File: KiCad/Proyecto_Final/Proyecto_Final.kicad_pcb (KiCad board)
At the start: 4 copper layers, 102 x 102 mm, 235 parts, among them J1 RF_IN, J10 PF, J11 PB, J12 PE, J13 PA, J14 PD, J15 SPI4, J16 OutEn, J17 CFG_SEL, J18 CTRL_MODE, J2 ADC_CLK_SEL, J3 5v, J4 I2C1, J5 ARM SWD, J6 USB_B_Micro, J7 Boot_Select, J8 PG, J9 PC, Q1 BSS315P, SW1 Reset, T1 B0310J50100AHF, T2 B0310J50100AHF, T3 2450BL05A0100, U1 SKY13351, U10 MAX2837, U11 TLV1117-33, U12 TPD4S012DRYR, U13 STM32F723ZCTx, U14 5P49V5929, U2 RFFC5072, U3 SKY13351, U4 SKY13351, U5 SKY13351, U6 SKY13351, U7 SKY13351, U8 MAAL-010200, U9 MAX1193ETI+, Y1 25MHz

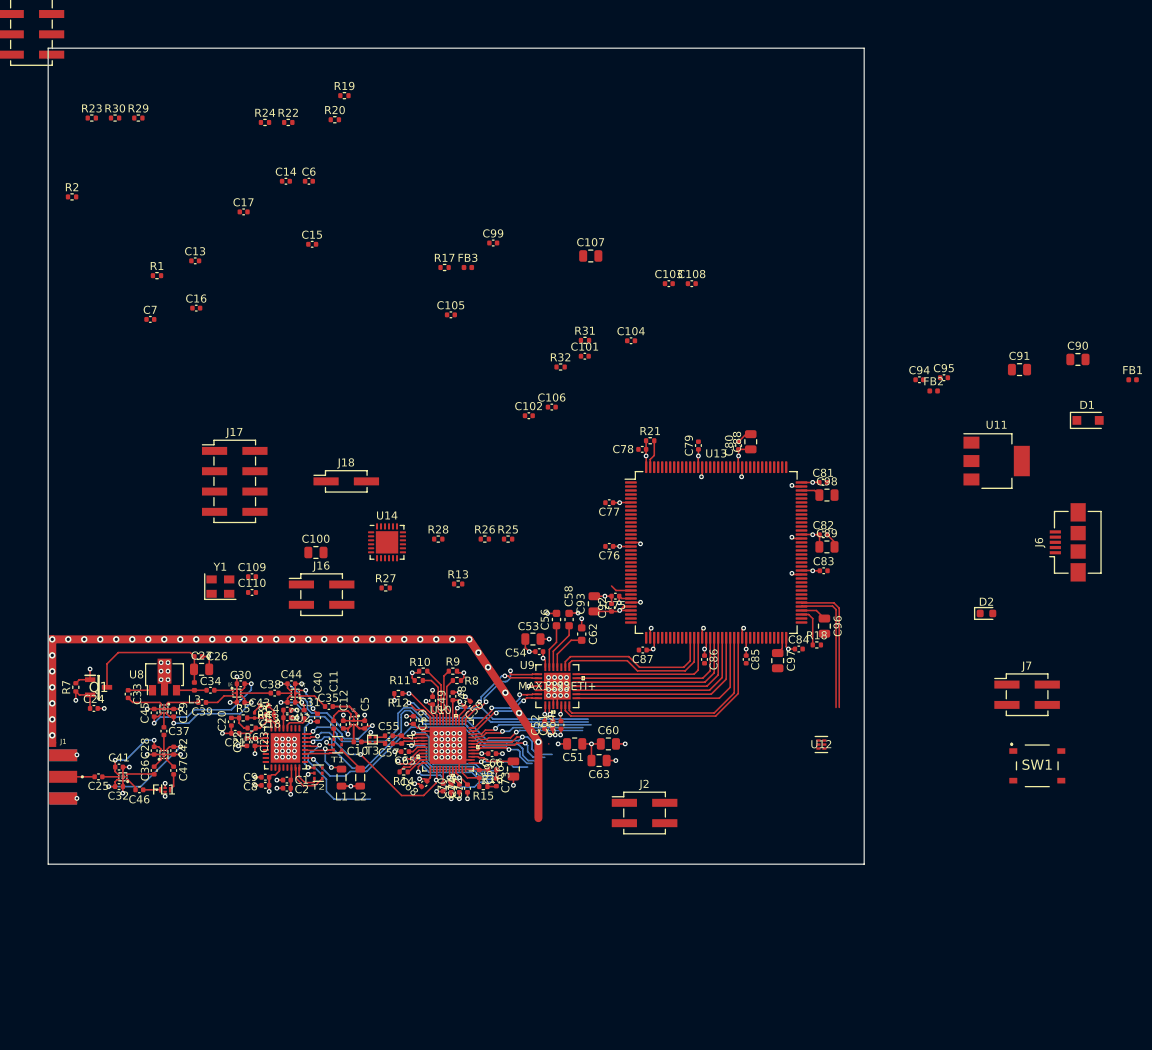
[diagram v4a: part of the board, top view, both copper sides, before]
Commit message: Reasignación de footprints por cambio de proveedor de componentes (JLCPCB SMT Assembly).
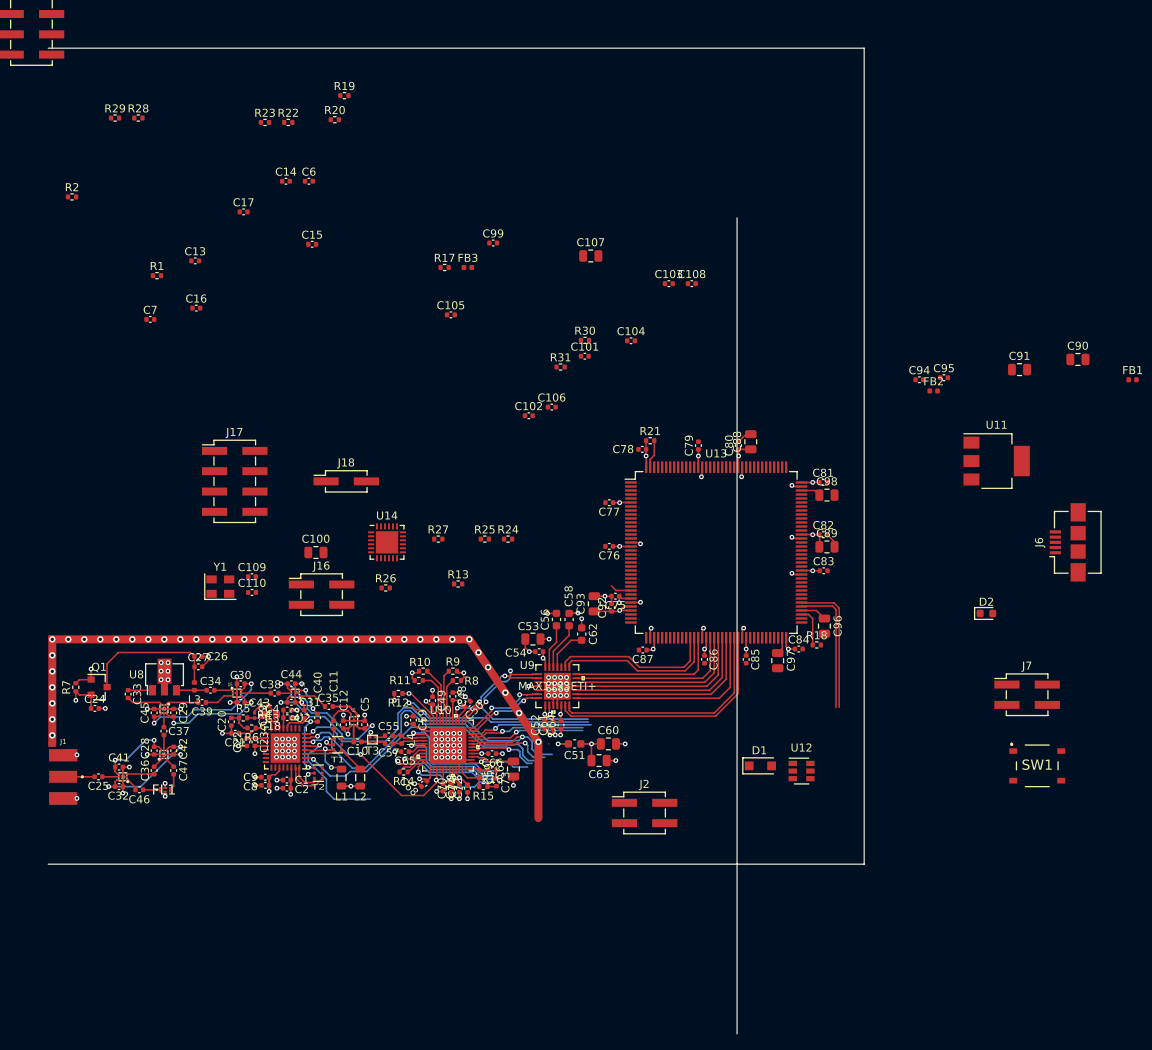
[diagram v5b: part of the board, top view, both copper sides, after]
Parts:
- removed the R23 at (81.2, 53.6)
- C18: footprint Capacitor_SMD:C_0402_1005Metric -> Capacitor_SMD:C_0603_1608Metric
- C27: footprint Capacitor_SMD:C_0805_2012Metric -> Capacitor_SMD:C_0402_1005Metric
- C51: footprint Capacitor_SMD:C_0805_2012Metric -> Capacitor_SMD:C_0603_1608Metric
- C52, C54, C61, C64: value 0.1uF -> 100nF
- D1: value PMEG2010EH -> SM4007
- FB1: value 120 @ 100MHz -> 600 @ 100MHz
- FB2, FB3: value 220 @ 100MHz -> 600 @ 100MHz
- Q1: value BSS315P -> Si2301CDS; footprint SamacSys_Parts:SOT95P237X112-3N -> Package_TO_SOT_SMD:SOT-23
- U12: value TPD4S012DRYR -> USBLC6-2SC6; footprint Tesis2020-21:TPD4S012DRYR -> Package_TO_SOT_SMD:SOT-23-6
- moved D1 59.5 mm to (164.8, 134.6)
- moved U12 4.14 mm to (169.9, 135.3)
- moved C27 0.52 mm to (94.5, 122.2)
- moved C24 0.13 mm to (81.6, 127.4)
- moved Q1 0.07 mm to (82.1, 124.8)
- renumbered R24 to R23, R25 to R24, R26 to R25, R27 to R26, R28 to R27, R29 to R28, R30 to R29, R31 to R30, R32 to R31
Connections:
- C100 pad 1: VDD_CLK -> VDDA_CLK
- C101 pad 1: VDD_CLK -> VDDA_CLK
- C102 pad 1: VDD_CLK -> VDDA_CLK
- C103 pad 1: VDD_CLK -> VDDA_CLK
- C104 pad 1: VDD_CLK -> VDDA_CLK
- C105 pad 1: VDD_CLK -> VDDA_CLK
- C106 pad 1: VDD_CLK -> VDDA_CLK
- FB1 pad 2: VBUS -> +5V
- FB3 pad 1: VDD_CLK -> VDDA_CLK
- J3 pad 1: VBUS -> +5V
- J6 pad 1: VBUS -> +5V
- J6 pad 2: USB_OTG_HS_D- -> USB_CONN_D-
- J6 pad 3: USB_OTG_HS_D+ -> USB_CONN_D+
- TP18 pad 1: VBUS -> +5V
- U12 pad 1: USB_OTG_HS_D+ -> USB_CONN_D+
- U12 pad 2: USB_OTG_HS_D- -> GND
- U12 pad 3: Net-(J6-Pad4) -> USB_CONN_D-
- U12 pad 4: GND -> USB_D-
- U12 pad 5: Net-(U12-Pad5) -> +5V
- U12 pad 6: VBUS -> USB_D+
- U13 pad 77: USB_OTG_HS_D- -> USB_D-
- U13 pad 78: USB_OTG_HS_D+ -> USB_D+
- U14 pad 10: VDD_CLK -> VDDA_CLK
- U14 pad 15: VDD_CLK -> VDDA_CLK
- U14 pad 18: VDD_CLK -> VDDA_CLK
- U14 pad 21: VDD_CLK -> VDDA_CLK
- U14 pad 22: VDD_CLK -> VDDA_CLK
- U14 pad 23: VDD_CLK -> VDDA_CLK
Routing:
- net USB_OTG_HS_D+: track 17.4 -> 0.00 mm
- net USB_D+: track 0.00 -> 17.4 mm
- net USB_OTG_HS_D-: track 16.7 -> 0.00 mm
- net USB_D-: track 0.00 -> 16.7 mm
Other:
- board size 102 x 102 mm -> 102 x 123.2 mm

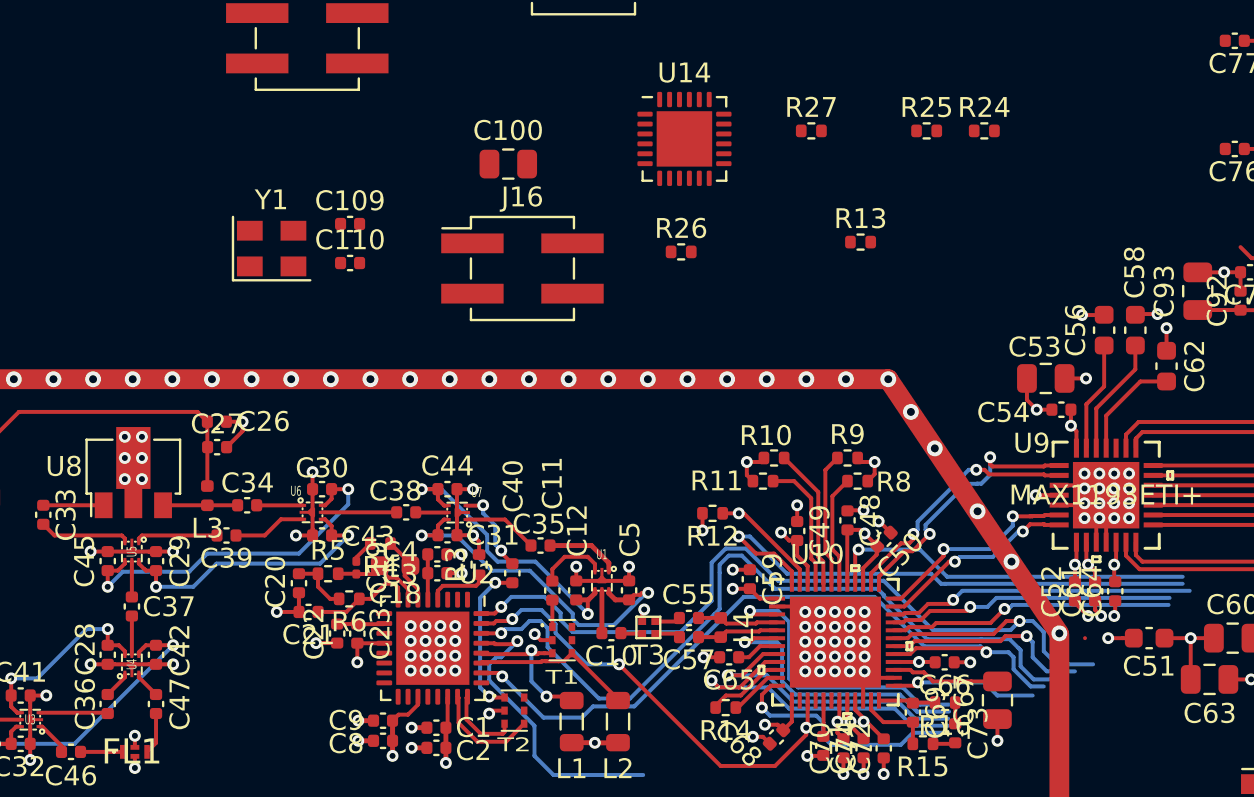
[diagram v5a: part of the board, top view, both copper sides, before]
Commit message: Agregada seccion de thermal vias.
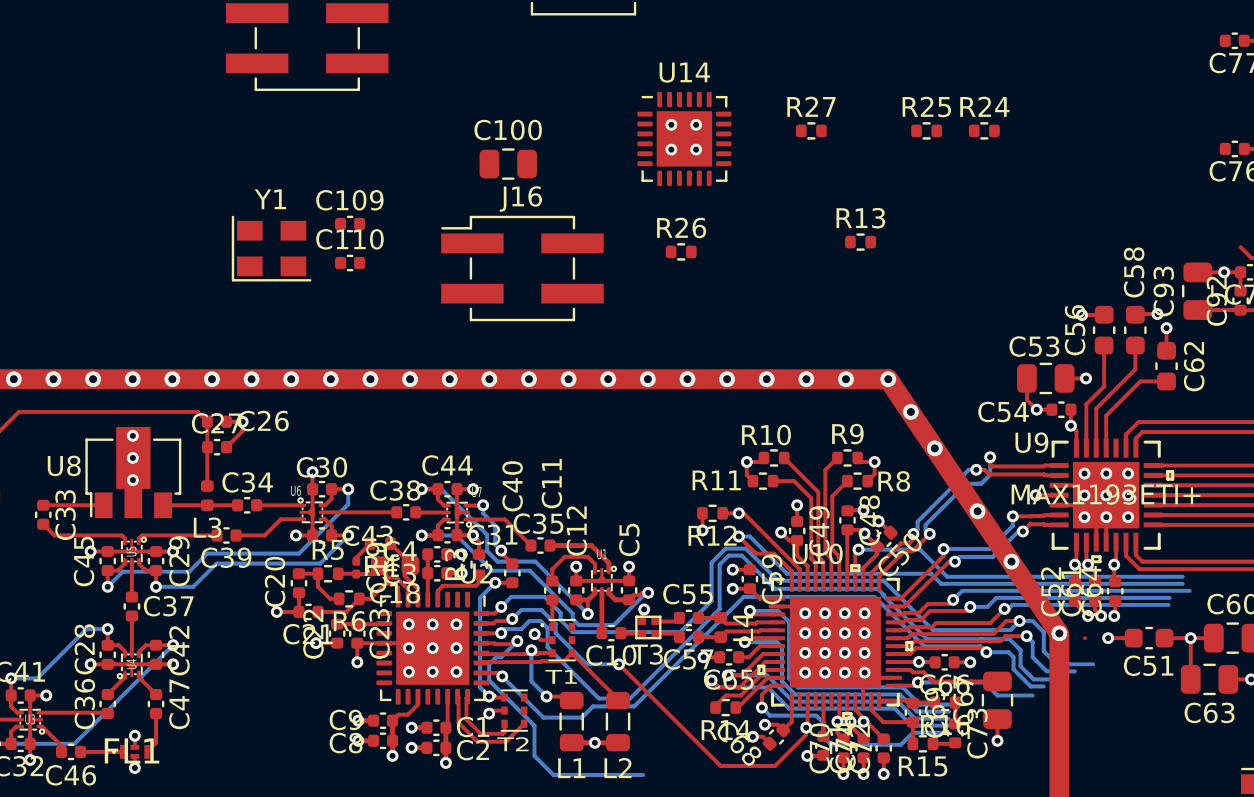
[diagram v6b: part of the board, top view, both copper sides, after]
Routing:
- net GND: track 107.4 -> 110.0 mm, vias 163 -> 141

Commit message: Avance PCB.
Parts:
- moved R1 70.3 mm to (113.6, 139.3), turned to 270 degrees
- moved C16 64.9 mm to (111.8, 139.9), turned to 180 degrees
- moved D1 56.1 mm to (202.9, 93.5)
- moved J6 49.7 mm to (166.6, 140.3), turned to 0 degrees
- moved J2 34.2 mm to (132.9, 111.0)
- moved C97 2.66 mm to (169.4, 122.6)
- moved C18 0.41 mm to (103.2, 128.0)
- moved R4 0.39 mm to (102.6, 126.7)
- moved C19 0.30 mm to (101.2, 128.3)
- moved C20 0.30 mm to (98.3, 129.1)
- moved C21 0.30 mm to (98.8, 130.6)
- moved R5 0.30 mm to (99.8, 128.6)
- moved R6 0.30 mm to (100.9, 129.9)
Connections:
- J13 pad 4: PA3 -> PC4
- U13 pad 10: Rx_Mix -> PF0
- U13 pad 11: Rx_Amp_Pwr -> PF1
- U13 pad 12: Rx_Amp_Bypass -> PF2
- U13 pad 123: B7 -> B1
- U13 pad 124: B6 -> B2
- U13 pad 125: B5 -> B3
- U13 pad 127: B3 -> B5
- U13 pad 128: B2 -> B7
- U13 pad 129: B1 -> B6
- U13 pad 13: Rx_Amp -> PF3
- U13 pad 14: Filt_Bypass -> PF4
- U13 pad 15: Filtro -> PF5
- U13 pad 37: PA3 -> SPI1_CS0
- U13 pad 44: SPI1_CS0 -> PC4
- U13 pad 46: Trx_Enable -> Trx_Rx_Enable
- U13 pad 47: Trx_Rx_Enable -> Trx_Enable
- U13 pad 64: PE11 -> Rx_Mix_Bypass
- U13 pad 65: PE12 -> Rx_Mix
- U13 pad 66: PE13 -> Rx_Amp_Bypass
- U13 pad 67: PE14 -> Rx_Amp
- U13 pad 68: PE15 -> Rx_Amp_Pwr
- U13 pad 69: PB10 -> Filt_Bypass
- U13 pad 7: Rx_Mix_Bypass -> PC13
- U13 pad 70: PB11 -> Filtro
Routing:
- net Rx_Amp_Pwr: track 3.32 -> 113.9 mm, vias 1 -> 2
- net Filt_Bypass: track 9.91 -> 109.1 mm, vias 2 -> 3
- net Rx_Amp: track 18.5 -> 116.6 mm, vias 2 -> 3
- net Filtro: track 15.1 -> 111.2 mm, vias 2 -> 3
- net Rx_Amp_Bypass: track 14.7 -> 107.3 mm, vias 2 -> 3
- net Rx_Mix: track 15.4 -> 106.0 mm, vias 2 -> 3
- net Rx_Mix_Bypass: track 18.5 -> 105.4 mm, vias 2 -> 3
- net B1: track 12.4 -> 78.8 mm, vias 1 -> 4
- net B2: track 16.9 -> 82.3 mm, vias 1 -> 4
- net B3: track 15.1 -> 79.4 mm, vias 1 -> 4
- net B4: track 14.5 -> 78.2 mm, vias 1 -> 4
- net B5: track 15.1 -> 76.5 mm, vias 1 -> 4
- net SPI1_SCK: track 22.6 -> 77.1 mm, vias 3 -> 6
- net B7: track 14.4 -> 59.8 mm, vias 1 -> 4
- net B6: track 15.4 -> 56.7 mm, vias 1 -> 4
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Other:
- board size 102 x 123.2 mm -> 102 x 102 mm

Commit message: Sección RF terminada.
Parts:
- removed the J2 at (132.9, 111.0)
- removed the R13 at (127.0, 111.9)
- removed the R2 at (78.7, 63.5)
- removed the R24 at (133.2, 106.3)
- added R22: 33, Resistor_SMD:R_0402_1005Metric, F.Cu at (130.9, 119.0)
- moved R21 62.7 mm to (132.6, 109.3)
- moved C108 47.7 mm to (122.2, 107.8), turned to 180 degrees
- moved C107 44.3 mm to (121.8, 109.5), turned to 180 degrees
- moved C103 40.0 mm to (131.2, 107.7), turned to 45 degrees
- moved FB3 33.2 mm to (137.5, 104.2), turned to 90 degrees
- moved C101 32.6 mm to (130.3, 113.5), turned to 270 degrees
- moved C104 31.3 mm to (130.5, 107.0), turned to 45 degrees
- moved C106 28.4 mm to (123.5, 113.8), turned to 225 degrees
- moved C105 28.2 mm to (129.7, 106.2), turned to 45 degrees
- moved Y1 25.5 mm to (121.6, 104.5), turned to 225 degrees
- moved R29 24.6 mm to (126.9, 105.8), turned to 135 degrees
- moved C100 23.9 mm to (132.9, 105.1), turned to 270 degrees
- moved J15 23.6 mm to (128.0, 98.0)
- moved C102 21.0 mm to (132.5, 111.6)
- moved C109 14.4 mm to (114.9, 106.5)
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- renumbered C17 to C13, C13 to C14, C14 to C15, C15 to C16, C16 to C17, J11 to J10, J12 to J11, J13 to J12, J14 to J13, J15 to J14, J16 to J15, J17 to J16, J18 to J17, J3 to J2, J4 to J3, J5 to J4, J6 to J5, J7 to J6, J8 to J7, J9 to J8, J10 to J9, R11 to R10, R12 to R11, R14 to R12, R15 to R13, R16 to R14, R17 to R15, R18 to R16, R19 to R17, R20 to R18, R21 to R19, R3 to R2, R22 to R20, R23 to R21, R25 to R23, R26 to R24, R27 to R25, R28 to R26, R29 to R27, R30 to R28, R31 to R29, R4 to R3, R5 to R4, R6 to R5, R7 to R6, R8 to R7, R9 to R8, R10 to R9
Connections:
- R21 pad 2: ADC_22MHz -> MCU_CLK
- R23 pad 2: MIX_CLK -> Trx_CLK
- R25 pad 2: Trx_CLK -> MIX_CLK
- R28 pad 2: MCU_CLK -> Clk_Out0
- R29 pad 2: MCU_CLK -> Clk_Out0
- TP31 pad 1: ADC_22MHz -> MCU_CLK
- TP32 pad 1: ADC_45MHz -> CLK_ADC
- TP33 pad 1: MIX_CLK -> Trx_CLK
- TP34 pad 1: Trx_CLK -> MIX_CLK
- TP35 pad 1: MCU_CLK -> Clk_Out0
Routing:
- net Trx_CLK: track 0.82 -> 37.5 mm, vias 1 -> 4
- net MIX_CLK: track 1.07 -> 36.4 mm, vias 1 -> 2
- net MCU_CLK: track 0.00 -> 35.0 mm
- net Net-(R22-Pad1): track 0.00 -> 26.0 mm
- net VDDA_CLK: track 0.00 -> 20.3 mm, vias 0 -> 7
- net CLK_ADC: track 1.18 -> 12.0 mm, vias 1 -> 2
- net XOUT: track 0.00 -> 8.92 mm
- net XIN: track 0.00 -> 5.66 mm
- net GND: track 110.0 -> 113.7 mm, vias 142 -> 130
- net SD_OE: track 0.00 -> 3.59 mm
- net MIX_IPN: track 3.85 -> 7.07 mm
- net I2C1_SDA: track 0.00 -> 3.12 mm, vias 0 -> 1
- net Net-(R21-Pad1): track 0.00 -> 3.08 mm
- net I2C1_SCL: track 0.00 -> 3.01 mm, vias 0 -> 1
- net /Frontend_analog/MIX_OPP: track 7.83 -> 10.6 mm
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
